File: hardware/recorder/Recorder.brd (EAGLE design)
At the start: 72.6 x 77.2 mm, 42 parts, among them T1 VN0109N3-G-ND, T2 IRF1404PBF, U1 DEV-16771_REDUCED_PINS, U2 MCP4822-E/P, U3 LM6132BIN, U4 Value, U5 L7808ABV, U6 L7908CV

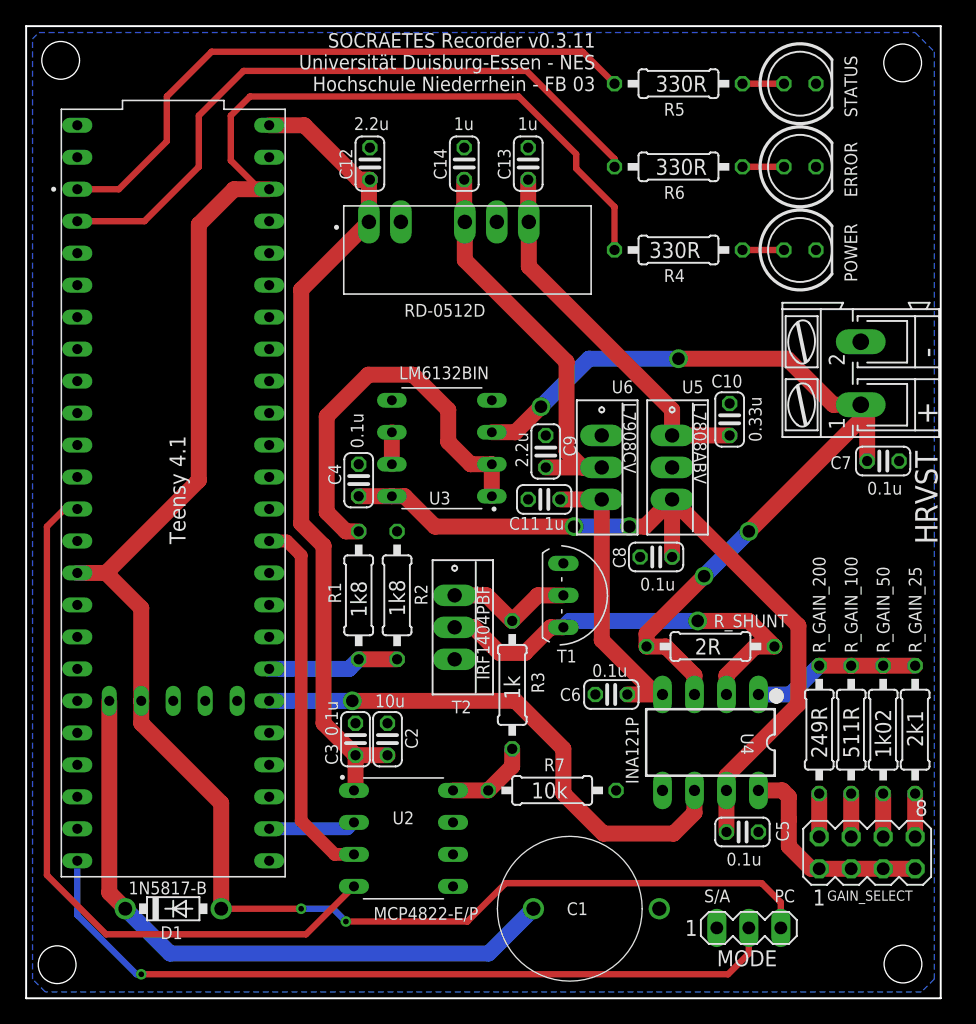
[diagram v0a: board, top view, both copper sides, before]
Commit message: change recorder layout to be more simple
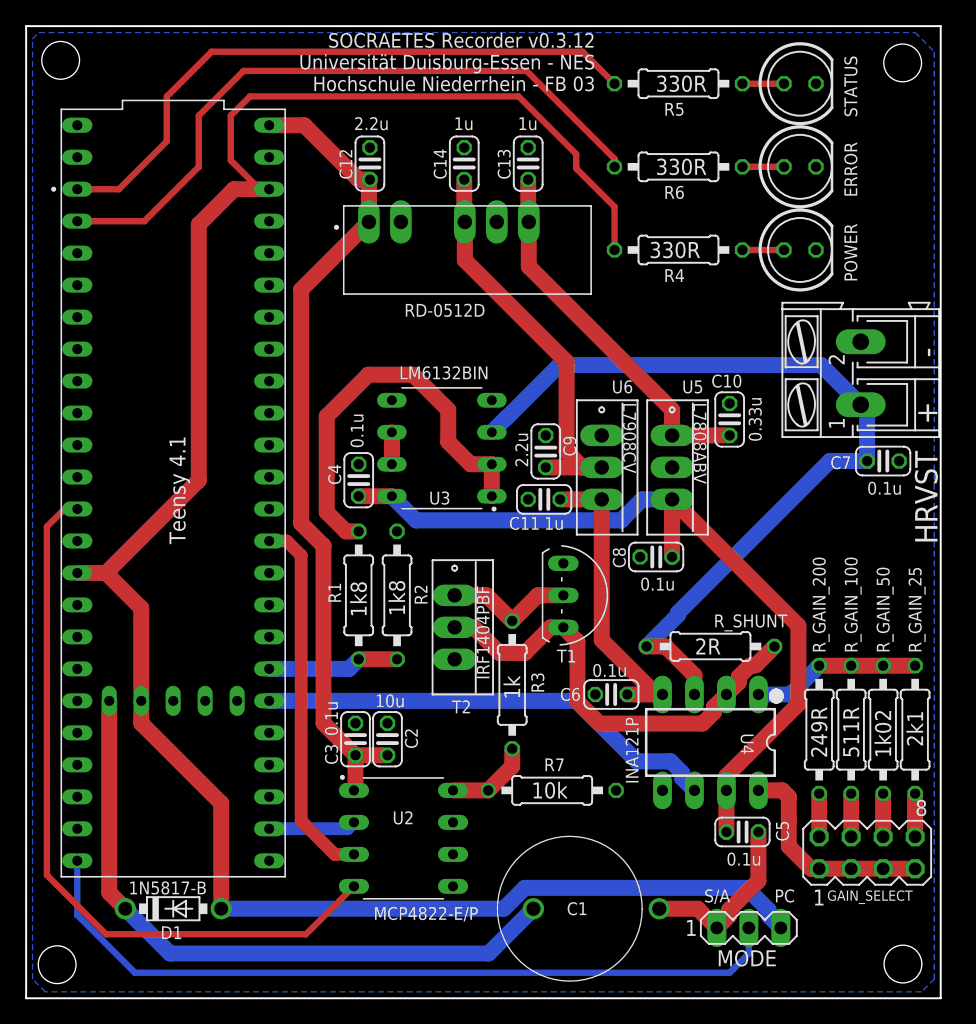
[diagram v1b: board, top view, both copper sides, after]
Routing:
- net GND: track 0.00 -> 14.2 mm
- net CURRENT_SENSE_AMP_OUTPUT: track 42.7 -> 37.0 mm, vias 1 -> 0
- net HARVESTER+: track 70.5 -> 67.5 mm, vias 4 -> 0
- net +3V3: track 165.4 -> 163.3 mm, vias 2 -> 0
- net N$6: track 34.4 -> 36.1 mm, vias 1 -> 0
- net +8V: track 64.3 -> 63.9 mm, vias 2 -> 0
- net JUMPER_SELECT_MODE: track 62.3 -> 62.2 mm, vias 1 -> 0
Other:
- board text added: "SOCRAETES Recorder v0.3.12 Universität Duisburg-Essen - NES Hochschule Niederrhein - FB 03"
- board text removed: "SOCRAETES Recorder v0.3.11 Universität Duisburg-Essen - NES Hochschule Niederrhein - FB 03"
